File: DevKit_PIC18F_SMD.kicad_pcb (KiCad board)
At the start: 2 copper layers, 27 x 51 mm, 25 parts, among them J1 PIC_ICSP_ICD, J2 USB_B_Mini, J5 RIGHT_PORT, J6 LEFT_PORT, SW1 SW_RST, X1 16MHz

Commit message: update images & comment.
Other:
- board text added: "DevKit PIC18F45XX SMD Rev.1 : 5th March, 2025 Designed by @deulamco"
- board text removed: "DevKit PIC18F45XX Rev.7 : 28th Feb, 2025 Designed by @deulamco"
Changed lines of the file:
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@@
 	(paper "A5")
 	(title_block
-		(comment 1 "Rev.3 : Remove bridge & re-route to fix USB-B power.")
-		(comment 2 "Rev.4 : Add Test LED, flip ICSP + move LED, Group all Resistors.")
-		(comment 3 "Rev.5 : Remove redundant LED D1.")
-		(comment 4 "Rev.6 : Fix LED D6 -> GND instead of pull-up VCC.")
-		(comment 5 "Rev.7 : Upgrade -> KiCAD 9.0.0 & fix GND.")
+		(comment 1 "Rev.1 : SMD version of DevKit 18F Rev.7 ")
 	)
 	(layers
@@
 		)
 	)
-	(gr_text "DevKit PIC18F45XX\nRev.7 : 28th Feb, 2025\nDesigned by @deulamco"
+	(gr_text "DevKit PIC18F45XX SMD\nRev.1 : 5th March, 2025\nDesigned by @deulamco"
 		(at 87.5 46.5 90)
 		(layer "B.SilkS")

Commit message: Added VCC/GND pins
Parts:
- J5, J6: footprint Connector_PinHeader_2.54mm:PinHeader_1x16_P2.54mm_Vertical -> Connector_PinHeader_2.54mm:PinHeader_1x17_P2.54mm_Vertical
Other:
- outline, holes or cut-outs redrawn
- board text removed: "UART"
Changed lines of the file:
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@@
 		)
 	)
-	(footprint "Connector_PinHeader_2.54mm:PinHeader_1x16_P2.54mm_Vertical"
+	(footprint "Connector_PinHeader_2.54mm:PinHeader_1x17_P2.54mm_Vertical"
 		(layer "B.Cu")
 		(at 93 33.96 180)
-		(descr "Through hole straight pin header, 1x16, 2.54mm pitch, single row")
-		(tags "Through hole pin header THT 1x16 2.54mm single row")
+		(descr "Through hole straight pin header, 1x17, 2.54mm pitch, single row")
+		(tags "Through hole pin header THT 1x17 2.54mm single row")
 		(property "Reference" "J5"
 			(at 0 2.33 0)
@@
 		)
 		(property "Value" "RIGHT_PORT"
-			(at 0 -40.43 0)
+			(at 0 -42.97 0)
 			(layer "B.Fab")
 			(effects
@@
 			)
 		)
-		(property "Description" "Generic connector, single row, 01x16, script generated"
+		(property "Description" "Generic connector, single row, 01x17, script generated"
 			(at 0 0 0)
 			(unlocked yes)
@@
 		(fp_line
 			(start 1.33 -1.27)
-			(end 1.33 -39.43)
+			(end 1.33 -41.97)
 			(stroke
 				(width 0.12)
@@
 		(fp_line
 			(start -1.33 -1.27)
-			(end -1.33 -39.43)
-			(stroke
-				(width 0.12)
-				(type solid)
-			)
-			(layer "B.SilkS")
-		)
-		(fp_line
-			(start -1.33 -39.43)
-			(end 1.33 -39.43)
+			(end -1.33 -41.97)
+			(stroke
+				(width 0.12)
+				(type solid)
+			)
+			(layer "B.SilkS")
+		)
+		(fp_line
+			(start -1.33 -41.97)
+			(end 1.33 -41.97)
 			(stroke
 				(width 0.12)
@@
 		)
 		(fp_line
-			(start 1.8 -39.9)
+			(start 1.8 -42.45)
 			(end 1.8 1.8)
 			(stroke
@@
 		(fp_line
 			(start -1.8 1.8)
-			(end -1.8 -39.9)
+			(end -1.8 -42.45)
 			(stroke
 				(width 0.05)
@@
 		)
 		(fp_line
-			(start -1.8 -39.9)
-			(end 1.8 -39.9)
+			(start -1.8 -42.45)
+			(end 1.8 -42.45)
 			(stroke
 				(width 0.05)
@@
 		(fp_line
 			(start 1.27 1.27)
-			(end 1.27 -39.37)
+			(end 1.27 -41.91)
 			(stroke
 				(width 0.1)
@@
 		)
 		(fp_line
-			(start 1.27 -39.37)
-			(end -1.27 -39.37)
+			(start 1.27 -41.91)
+			(end -1.27 -41.91)
 			(stroke
 				(width 0.1)
@@
 		)
 		(fp_line
-			(start -1.27 -39.37)
+			(start -1.27 -41.91)
 			(end -1.27 0.635)
 			(stroke
@@
 		)
 		(fp_text user "${REFERENCE}"
-			(at 0 -19.05 90)
+			(at 0 -20.32 90)
 			(layer "B.Fab")
 			(effects
@@
 			(pintype "passive")
 		)
+		(pad "17" thru_hole oval
+			(at 0 -40.64 180)
+			(size 1.7 1.7)
+			(drill 1)
+			(layers "*.Cu" "*.Mask")
+			(remove_unused_layers no)
+			(net 2 "GND")
+			(pinfunction "Pin_17")
+			(pintype "passive")
+		)
 		(embedded_fonts no)
-		(model "${KICAD9_3DMODEL_DIR}/Connector_PinHeader_2.54mm.3dshapes/PinHeader_1x16_P2.54mm_Vertical.wrl"
+		(model "${KICAD9_3DMODEL_DIR}/Connector_PinHeader_2.54mm.3dshapes/PinHeader_1x17_P2.54mm_Vertical.wrl"
 			(offset
 				(xyz 0 0 0)
@@
 		)
 	)
-	(footprint "Connector_PinHeader_2.54mm:PinHeader_1x16_P2.54mm_Vertical"
+	(footprint "Connector_PinHeader_2.54mm:PinHeader_1x17_P2.54mm_Vertical"
 		(layer "B.Cu")
 		(at 77.5 34 180)
-		(descr "Through hole straight pin header, 1x16, 2.54mm pitch, single row")
-		(tags "Through hole pin header THT 1x16 2.54mm single row")
+		(descr "Through hole straight pin header, 1x17, 2.54mm pitch, single row")
+		(tags "Through hole pin header THT 1x17 2.54mm single row")
 		(property "Reference" "J6"
 			(at 0 2.33 0)
@@
 		)
 		(property "Value" "LEFT_PORT"
-			(at 0 -40.43 0)
+			(at 0 -42.97 0)
 			(layer "B.Fab")
 			(effects
@@
 			)
 		)
-		(property "Description" "Generic connector, single row, 01x16, script generated"
+		(property "Description" "Generic connector, single row, 01x17, script generated"
 			(at 0 0 0)
 			(unlocked yes)
@@
 		(fp_line
 			(start 1.33 -1.27)
-			(end 1.33 -39.43)
+			(end 1.33 -41.97)
 			(stroke
 				(width 0.12)
@@
 		(fp_line
 			(start -1.33 -1.27)
-			(end -1.33 -39.43)
-			(stroke
-				(width 0.12)
-				(type solid)
-			)
-			(layer "B.SilkS")
-		)
-		(fp_line
-			(start -1.33 -39.43)
-			(end 1.33 -39.43)
+			(end -1.33 -41.97)
+			(stroke
+				(width 0.12)
+				(type solid)
+			)
+			(layer "B.SilkS")
+		)
+		(fp_line
+			(start -1.33 -41.97)
+			(end 1.33 -41.97)
 			(stroke
 				(width 0.12)
@@
 		)
 		(fp_line
-			(start 1.8 -39.9)
+			(start 1.8 -42.45)
 			(end 1.8 1.8)
 			(stroke
@@
 		(fp_line
 			(start -1.8 1.8)
-			(end -1.8 -39.9)
+			(end -1.8 -42.45)
 			(stroke
 				(width 0.05)
@@
 		)
 		(fp_line
-			(start -1.8 -39.9)
-			(end 1.8 -39.9)
+			(start -1.8 -42.45)
+			(end 1.8 -42.45)
 			(stroke
 				(width 0.05)
@@
 		(fp_line
 			(start 1.27 1.27)
-			(end 1.27 -39.37)
+			(end 1.27 -41.91)
 			(stroke
 				(width 0.1)
@@
 		)
 		(fp_line
-			(start 1.27 -39.37)
-			(end -1.27 -39.37)
+			(start 1.27 -41.91)
+			(end -1.27 -41.91)
 			(stroke
 				(width 0.1)
@@
 		)
 		(fp_line
-			(start -1.27 -39.37)
+			(start -1.27 -41.91)
 			(end -1.27 0.635)
 			(stroke
@@
 		)
 		(fp_text user "${REFERENCE}"
-			(at 0 -19.05 90)
+			(at 0 -20.32 90)
 			(layer "B.Fab")
 			(effects
@@
 			(pintype "passive")
 		)
+		(pad "17" thru_hole oval
+			(at 0 -40.64 180)
+			(size 1.7 1.7)
+			(drill 1)
+			(layers "*.Cu" "*.Mask")
+			(remove_unused_layers no)
+			(net 6 "VCC")
+			(pinfunction "Pin_17")
+			(pintype "passive")
+		)
 		(embedded_fonts no)
-		(model "${KICAD9_3DMODEL_DIR}/Connector_PinHeader_2.54mm.3dshapes/PinHeader_1x16_P2.54mm_Vertical.wrl"
+		(model "${KICAD9_3DMODEL_DIR}/Connector_PinHeader_2.54mm.3dshapes/PinHeader_1x17_P2.54mm_Vertical.wrl"
 			(offset
 				(xyz 0 0 0)
@@
 	)
 	(gr_circle
-		(center 75.516361 30.016361)
-		(end 76.516361 30.016361)
+		(center 75 29.5)
+		(end 75.483639 29.483639)
 		(stroke
 			(width 0.05)
@@
 	)
 	(gr_circle
-		(center 95.5 74.386652)
-		(end 95.9937 75.384552)
+		(center 85 75.5)
+		(end 85.4937 76.113348)
 		(stroke
 			(width 0.05)
@@
 		(fill no)
 		(layer "Edge.Cuts")
+	)
+	(gr_text "GND"
+		(at 95 75 0)
+		(layer "F.SilkS")
+		(effects
+			(font
+				(size 1 1)
+				(thickness 0.125)
+			)
+			(justify left bottom)
+		)
+	)
+	(gr_text "VCC"
+		(at 73.5 75 0)
+		(layer "F.SilkS")
+		(effects
+			(font
+				(size 1 1)
+				(thickness 0.125)
+			)
+			(justify left bottom)
+		)
 	)
 	(gr_text "RA5"
@@
 				(bold yes)
 			)
-			(justify left bottom)
-		)
-	)
-	(gr_text "UART"
-		(at 73 74.5 0)
-		(layer "F.SilkS" knockout)
-		(effects
-			(font
-				(size 1 1.25)
-				(thickness 0.2)
-				(bold yes)
-			)

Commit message: Remove PWR flag in Reset part, since we updated wrong pin setup in symbol PIC18F45K50.
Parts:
- C5: value 10uF -> 100nF
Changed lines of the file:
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@@
 			(net 9 "/MCLR")
 			(pinfunction "RE3/VPP/*MCLR")
-			(pintype "power_in")
+			(pintype "input")
 		)
 		(pad "2" smd roundrect
@@
 			)
 		)
-		(property "Value" "10uF"
+		(property "Value" "100nF"
 			(at 0 1.85 90)
 			(layer "F.Fab")

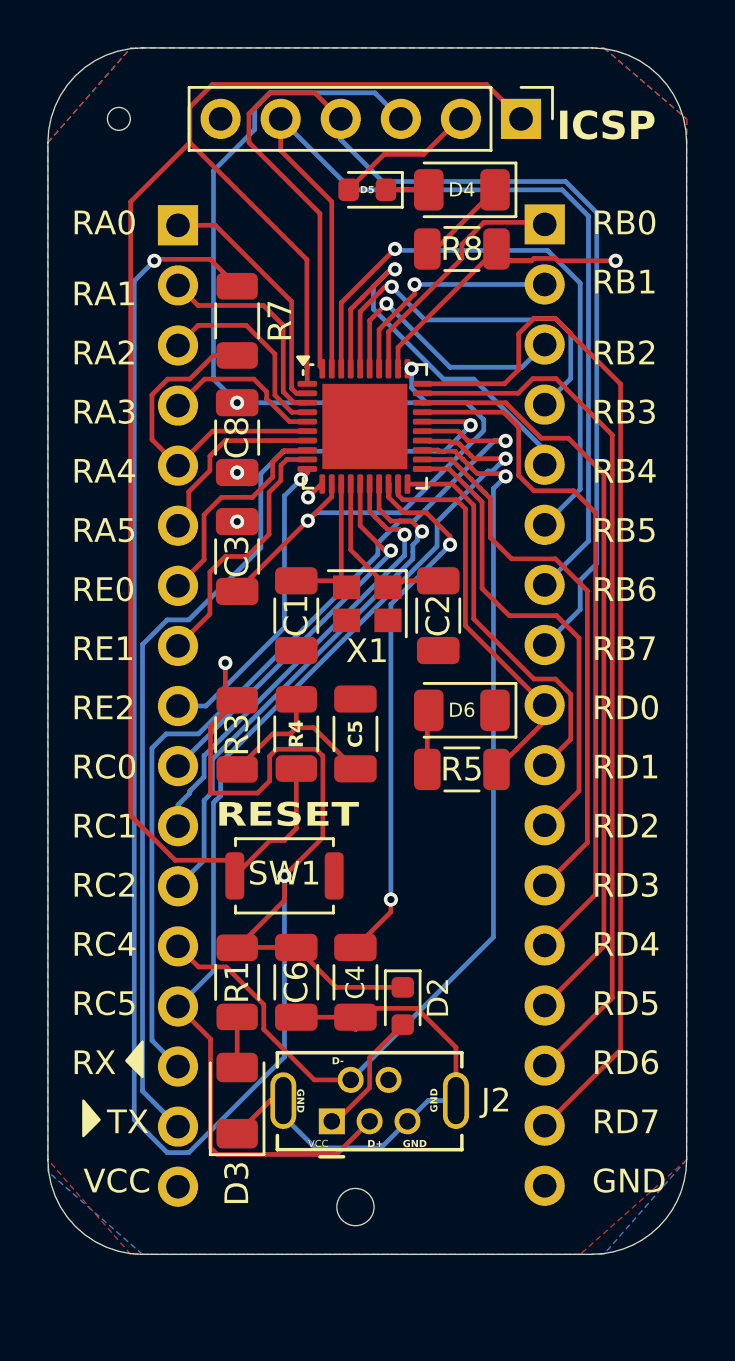
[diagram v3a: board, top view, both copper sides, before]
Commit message: rev.2 : and GND -> Left sockets & move RST_Button to bottom.
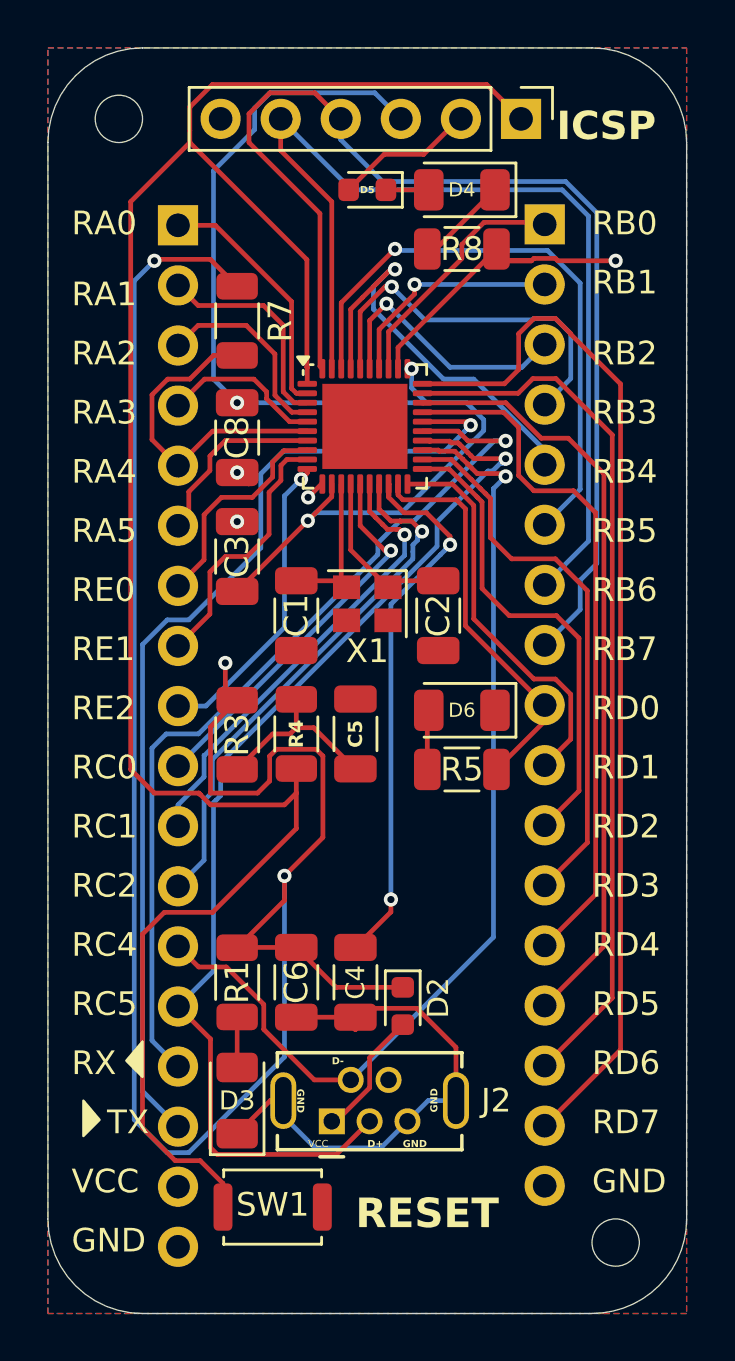
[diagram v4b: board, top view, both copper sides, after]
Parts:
- J6: footprint Connector_PinHeader_2.54mm:PinHeader_1x17_P2.54mm_Vertical -> Connector_PinHeader_2.54mm:PinHeader_1x18_P2.54mm_Vertical
- moved SW1 14.0 mm to (81.5, 75.5)
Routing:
- net /MCLR: track 69.4 -> 88.7 mm
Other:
- board size 27 x 51 mm -> 27 x 53.5 mm
- board text added: "DevKit_SMD PIC18F45K50 Rev.2 : 7th March, 2025 Designed by @deulamco"
- board text removed: "DevKit PIC18F45XX SMD Rev.1 : 5th March, 2025 Designed by @deulamco"
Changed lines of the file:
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@@
 	(title_block
 		(comment 1 "Rev.1 : SMD version of DevKit 18F Rev.7 ")
+		(comment 2 "Rev.2 : Add GND & move RST button to bottom")
 	)
 	(layers
@@
 			(drillshape 0)
 			(scaleselection 1)
-			(outputdirectory "../../../Downloads/FAB_DevKit_PIC18F/")
+			(outputdirectory "../../../Downloads/FAB_DevKit_PIC18F_SMD/")
 		)
 	)
@@
 		(tags "LED")
 		(property "Reference" "D3"
-			(at -3.5 0 90)
+			(at 0 0 180)
 			(layer "F.SilkS")
 			(effects
 				(font
-					(size 1 1)
+					(size 0.8 0.8)
 					(thickness 0.15)
 				)
@@
 	(footprint "Button_Switch_SMD:SW_Push_SPST_NO_Alps_SKRK"
 		(layer "F.Cu")
-		(at 82 61.5)
+		(at 81.5 75.5)
 		(descr "http://www.alps.com/prod/info/E/HTML/Tact/SurfaceMount/SKRK/SKRKAHE020.html")
 		(tags "SMD SMT button")
@@
 		)
 	)
-	(footprint "Connector_PinHeader_2.54mm:PinHeader_1x17_P2.54mm_Vertical"
+	(footprint "Connector_PinHeader_2.54mm:PinHeader_1x18_P2.54mm_Vertical"
 		(layer "B.Cu")
 		(at 77.5 34 180)
-		(descr "Through hole straight pin header, 1x17, 2.54mm pitch, single row")
-		(tags "Through hole pin header THT 1x17 2.54mm single row")
+		(descr "Through hole straight pin header, 1x18, 2.54mm pitch, single row")
+		(tags "Through hole pin header THT 1x18 2.54mm single row")
 		(property "Reference" "J6"
 			(at 0 2.33 0)
@@
 		)
 		(property "Value" "LEFT_PORT"
-			(at 0 -42.97 0)
+			(at 0 -45.51 0)
 			(layer "B.Fab")
 			(effects
@@
 			)
 		)
-		(property "Description" "Generic connector, single row, 01x17, script generated"
+		(property "Description" "Generic connector, single row, 01x18, script generated"
 			(at 0 0 0)
 			(unlocked yes)
@@
 		(fp_line
 			(start 1.33 -1.27)
-			(end 1.33 -41.97)
+			(end 1.33 -44.51)
 			(stroke
 				(width 0.12)
@@
 		(fp_line
 			(start -1.33 -1.27)
-			(end -1.33 -41.97)
+			(end -1.33 -44.51)
 			(stroke
 				(width 0.12)
@@
 		)
 		(fp_line
-			(start -1.33 -41.97)
-			(end 1.33 -41.97)
+			(start -1.33 -44.51)
+			(end 1.33 -44.51)
 			(stroke
 				(width 0.12)
@@
 		)
 		(fp_line
-			(start 1.8 -42.45)
+			(start 1.8 -44.95)
 			(end 1.8 1.8)
 			(stroke
@@
 		(fp_line
 			(start -1.8 1.8)
-			(end -1.8 -42.45)
+			(end -1.8 -44.95)
 			(stroke
 				(width 0.05)
@@
 		)
 		(fp_line
-			(start -1.8 -42.45)
-			(end 1.8 -42.45)
+			(start -1.8 -44.95)
+			(end 1.8 -44.95)
 			(stroke
 				(width 0.05)
@@
 		(fp_line
 			(start 1.27 1.27)
-			(end 1.27 -41.91)
+			(end 1.27 -44.45)
 			(stroke
 				(width 0.1)
@@
 		)
 		(fp_line
-			(start 1.27 -41.91)
-			(end -1.27 -41.91)
+			(start 1.27 -44.45)
+			(end -1.27 -44.45)
 			(stroke
 				(width 0.1)
@@
 		)
 		(fp_line
-			(start -1.27 -41.91)
+			(start -1.27 -44.45)
 			(end -1.27 0.635)
 			(stroke
@@
 		)
 		(fp_text user "${REFERENCE}"
-			(at 0 -20.32 90)
+			(at 0 -21.59 90)
 			(layer "B.Fab")
 			(effects
@@
 			(pintype "passive")
 		)
+		(pad "18" thru_hole oval
+			(at 0 -43.18 180)
+			(size 1.7 1.7)
+			(drill 1)
+			(layers "*.Cu" "*.Mask")
+			(remove_unused_layers no)
+			(net 2 "GND")
+			(pinfunction "Pin_18")
+			(pintype "passive")
+		)
 		(embedded_fonts no)
-		(model "${KICAD9_3DMODEL_DIR}/Connector_PinHeader_2.54mm.3dshapes/PinHeader_1x17_P2.54mm_Vertical.wrl"
+		(model "${KICAD9_3DMODEL_DIR}/Connector_PinHeader_2.54mm.3dshapes/PinHeader_1x18_P2.54mm_Vertical.wrl"
 			(offset
 				(xyz 0 0 0)
@@
 	)
 	(gr_circle
-		(center 75 29.5)
-		(end 75.483639 29.483639)
+		(center 75 29.499866)
+		(end 76 29.499866)
 		(stroke
 			(width 0.05)
-			(type default)
+			(type solid)
 		)
 		(fill no)
@@
 	)
 	(gr_line
-		(start 72 73.5)
+		(start 72 76)
 		(end 72 30.5)
 		(stroke
@@
 	)
 	(gr_arc
-		(start 76 77.5)
-		(mid 73.171573 76.328427)
-		(end 72 73.5)
+		(start 76 80)
+		(mid 73.171573 78.828427)
+		(end 72 76)
 		(stroke
 			(width 0.05)
@@
 	)
 	(gr_line
-		(start 95 77.5)
-		(end 76 77.5)
+		(start 95 80)
+		(end 76 80)
 		(stroke
 			(width 0.05)
@@
 	)
 	(gr_arc
-		(start 99 73.5)
-		(mid 97.831719 76.324667)
-		(end 95.008274 77.495862)
+		(start 99 76)
+		(mid 97.831719 78.824667)
+		(end 95.008274 79.995862)
 		(stroke
 			(width 0.05)
@@
 	(gr_line
 		(start 99 30.5)
-		(end 99 73.5)
+		(end 99 76)
 		(stroke
 			(width 0.05)
@@
 	)
 	(gr_circle
-		(center 85 75.5)
-		(end 85.4937 76.113348)
+		(center 96 77)
+		(end 97 77)
 		(stroke
 			(width 0.05)
-			(type default)
+			(type solid)
 		)
 		(fill no)
@@
 	)
 	(gr_text "VCC"
-		(at 73.5 75 0)
+		(at 73 75 0)
 		(layer "F.SilkS")
 		(effects
@@
 	)
 	(gr_text "RESET"
-		(at 79.09 59.5 0)
+		(at 85 76.5 0)
 		(layer "F.SilkS" knockout)
 		(effects
 			(font
-				(size 1 1.25)
+				(size 1.25 1.25)
 				(thickness 0.2)
 				(bold yes)
@@
 	)
 	(gr_text "GND"
+		(at 73 77.5 0)
+		(layer "F.SilkS")
+		(effects
+			(font
+				(size 1 1)
+				(thickness 0.125)
+			)
+			(justify left bottom)
+		)
+	)
+	(gr_text "GND"
 		(at 82.5 70.5 270)
 		(layer "F.SilkS")
@@
 		)
 	)
-	(gr_text "DevKit PIC18F45XX SMD\nRev.1 : 5th March, 2025\nDesigned by @deulamco"
-		(at 87.5 46.5 90)
+	(gr_text "DevKit_SMD PIC18F45K50\nRev.2 : 7th March, 2025\nDesigned by @deulamco"
+		(at 87.5 45 90)
 		(layer "B.SilkS")
 		(effects
@@
 	)
 	(segment
-		(start 82.5 56.9625)
-		(end 82.5 59.5)
+		(start 78.37761 58)
+		(end 78.438805 58.061195)
+		(width 0.2)
+		(layer "F.Cu")
+		(net 9)
+	)
+	(segment
+		(start 78.87761 58.5)
+		(end 82 58.5)
+		(width 0.2)
+		(layer "F.Cu")
+		(net 9)
+	)
+	(segment
+		(start 77.38195 73.539)
+		(end 78.439 73.539)
+		(width 0.2)
+		(layer "F.Cu")
+		(net 9)
+	)
+	(segment
+		(start 78.439 73.539)
+		(end 79.4 74.5)
 		(width 0.2)
 		(layer "F.Cu")
@@
 	)
 	(segment
+		(start 78 30.5)
+		(end 75.5 33)
+		(width 0.2)
+		(layer "F.Cu")
+		(net 9)
+	)
+	(segment
+		(start 76.920475 63.041)
+		(end 76 63.961475)
+		(width 0.2)
+		(layer "F.Cu")
+		(net 9)
+	)
+	(segment
+		(start 78.438805 58.061195)
+		(end 78.87761 58.5)
+		(width 0.2)
+		(layer "F.Cu")
+		(net 9)
+	)
+	(segment
 		(start 82.951333 40.000779)
 		(end 82.9625 40.011946)
@@
 	)
 	(segment
-		(start 82 60)
-		(end 81.4 60)
+		(start 82.5 58)
+		(end 82.5 59.5)
 		(width 0.2)
 		(layer "F.Cu")
@@
 	)
 	(segment
-		(start 79.9 60.839)
-		(end 77.38195 60.839)
+		(start 82 58.5)
+		(end 82.5 58)
+		(width 0.2)
+		(layer "F.Cu")
+		(net 9)
+	)
+	(segment
+		(start 82.5 56.9625)
+		(end 82.5 58)
 		(width 0.2)
 		(layer "F.Cu")
@@
 	)
 	(segment
-		(start 81.4 60)
-		(end 79.9 61.5)
+		(start 75.5 57)
+		(end 76.5 58)
 		(width 0.2)
 		(layer "F.Cu")
@@
 	)
 	(segment
+		(start 78.959 63.041)
+		(end 76.920475 63.041)
+		(width 0.2)
+		(layer "F.Cu")
+		(net 9)
+	)
+	(segment
+		(start 76 72.15705)
+		(end 77.38195 73.539)
+		(width 0.2)
+		(layer "F.Cu")
+		(net 9)
+	)
+	(segment
 		(start 90.548 28.048)
 		(end 92 29.5)
@@
 	)
 	(segment
+		(start 82.5 59.5)
+		(end 78.959 63.041)
+		(width 0.2)
+		(layer "F.Cu")
+		(net 9)
+	)
+	(segment
+		(start 78.377611 58)
+		(end 78.438805 58.061195)
+		(width 0.2)
+		(layer "F.Cu")
+		(net 9)
+	)
+	(segment
 		(start 78.952 28.048)
 		(end 90.548 28.048)
@@
 	)
 	(segment
-		(start 82.5 59.5)
-		(end 82 60)
+		(start 76.5 58)
+		(end 78.37761 58)
 		(width 0.2)
 		(layer "F.Cu")
@@
 	)
 	(segment
-		(start 77.38195 60.839)
-		(end 75.5 58.95705)
+		(start 75.5 33)
+		(end 75.5 57)
 		(width 0.2)
 		(layer "F.Cu")
@@
 	)
 	(segment
-		(start 75.5 58.95705)
-		(end 75.5 33)
+		(start 76 63.961475)
+		(end 76 72.15705)
 		(width 0.2)
 		(layer "F.Cu")
@@
 	)
 	(segment
-		(start 82.9625 40.011946)
-		(end 82.9625 40.7)
+		(start 79.4 74.5)
+		(end 79.4 75.5)
 		(width 0.2)
 		(layer "F.Cu")
@@
 	)
 	(segment
-		(start 75.5 33)
-		(end 78 30.5)
+		(start 82.9625 40.011946)
+		(end 82.9625 40.7)
 		(width 0.2)
 		(layer "F.Cu")
@@
 		(polygon
 			(pts
-				(xy 75.5 26.5) (xy 95.5 26.5) (xy 99 29.5) (xy 99 73.5) (xy 94.5 77.5) (xy 75.5 77.5) (xy 72 73.5)
-				(xy 72 30.5)
+				(xy 72 26.5) (xy 99 26.5) (xy 99 26.5) (xy 99 80) (xy 95.5 80) (xy 75.5 80) (xy 72 80) (xy 72 26.5)
 			)
 		)
@@
 		(polygon
 			(pts
-				(xy 75.5 26.5) (xy 95.5 26.5) (xy 99 29.5) (xy 99 73.5) (xy 95.5 77.5) (xy 76 77.5) (xy 72 74) (xy 72 30.5)
+				(xy 72 26.5) (xy 99 26.5) (xy 99 26.5) (xy 99 80) (xy 99 80) (xy 72 80) (xy 72 80) (xy 72 26.5)
 			)
 		)
